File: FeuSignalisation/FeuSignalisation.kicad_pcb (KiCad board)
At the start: 2 copper layers, 77 x 35.8 mm, 17 parts, among them K1 12VAC, K2 ENTREES, K3 SORTIES, K4 RES

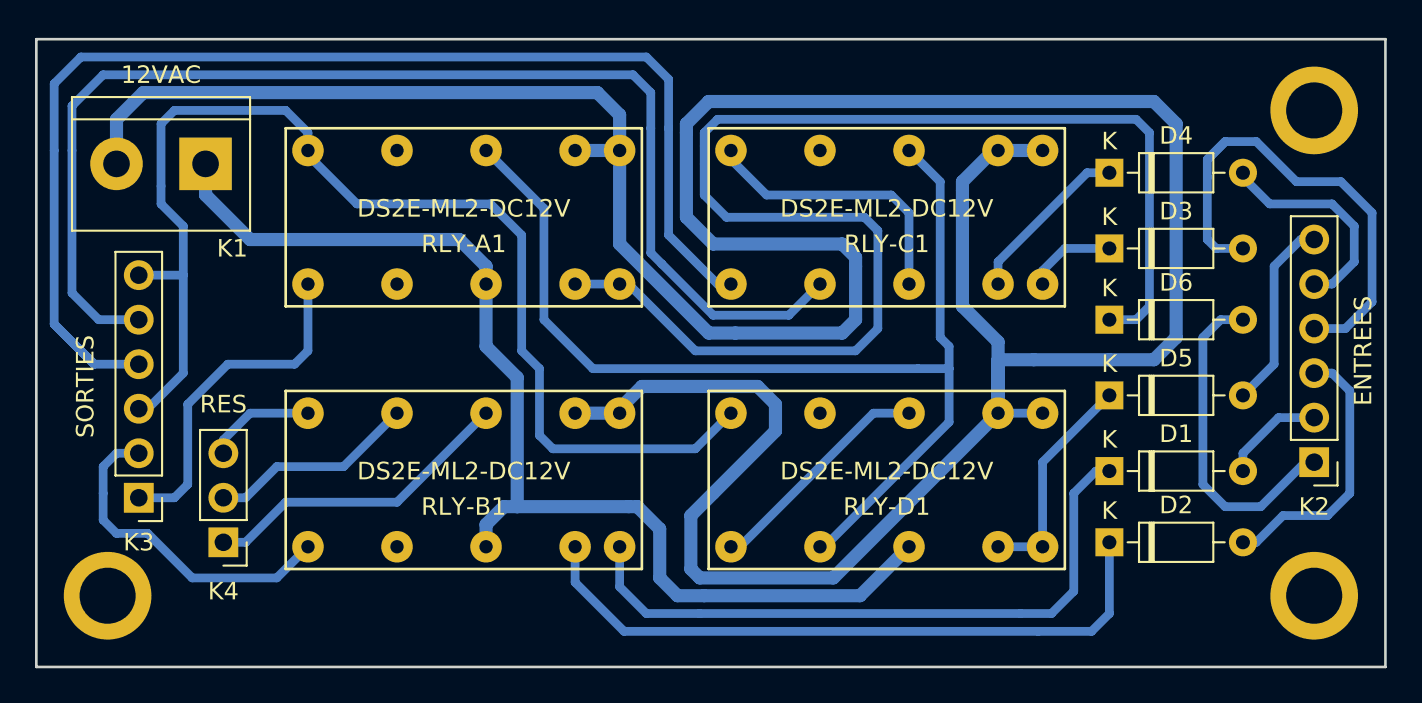
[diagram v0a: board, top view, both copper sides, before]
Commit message: Corrections
Une erreur + changement des pastilles pour réalisation à la main plus facile + ajout du nom des cartes coté soudure
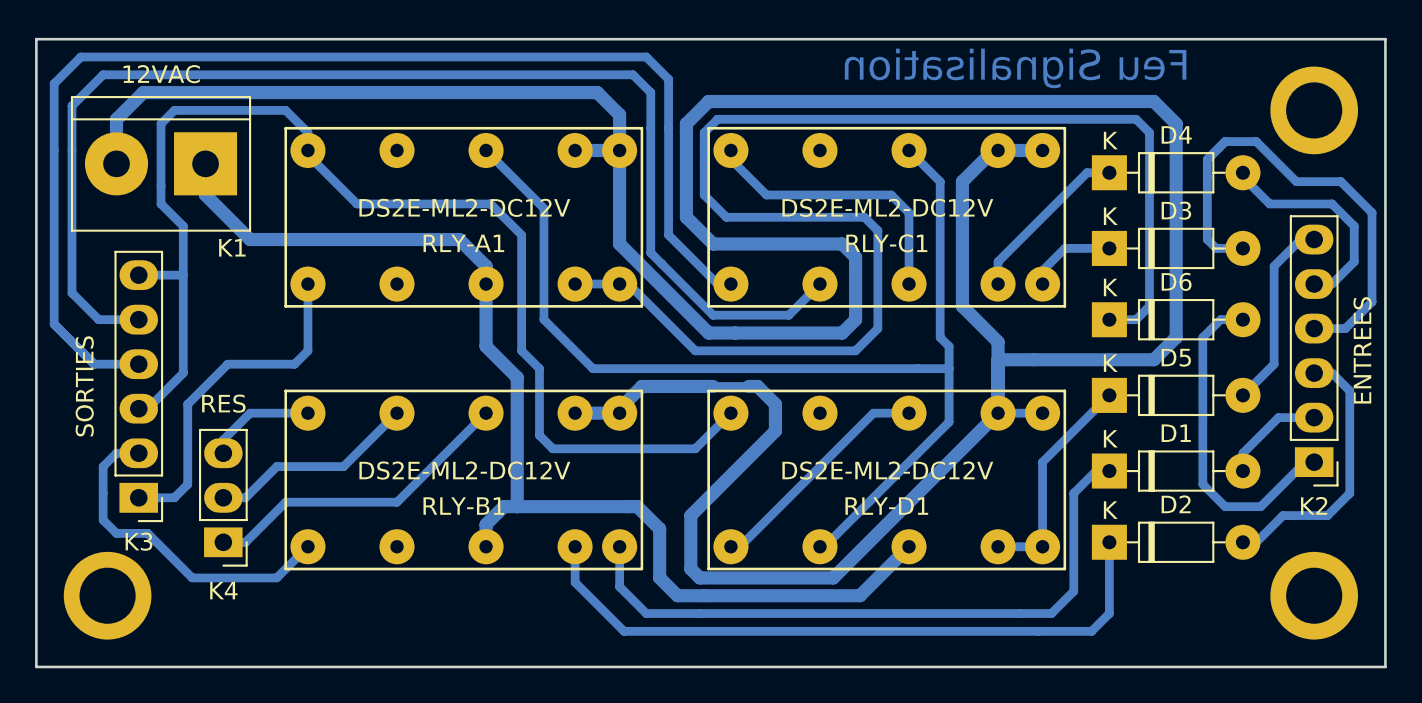
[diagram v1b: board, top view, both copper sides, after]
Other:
- board text added: "Feu Signalisation"
